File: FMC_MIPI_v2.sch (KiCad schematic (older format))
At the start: 0 parts

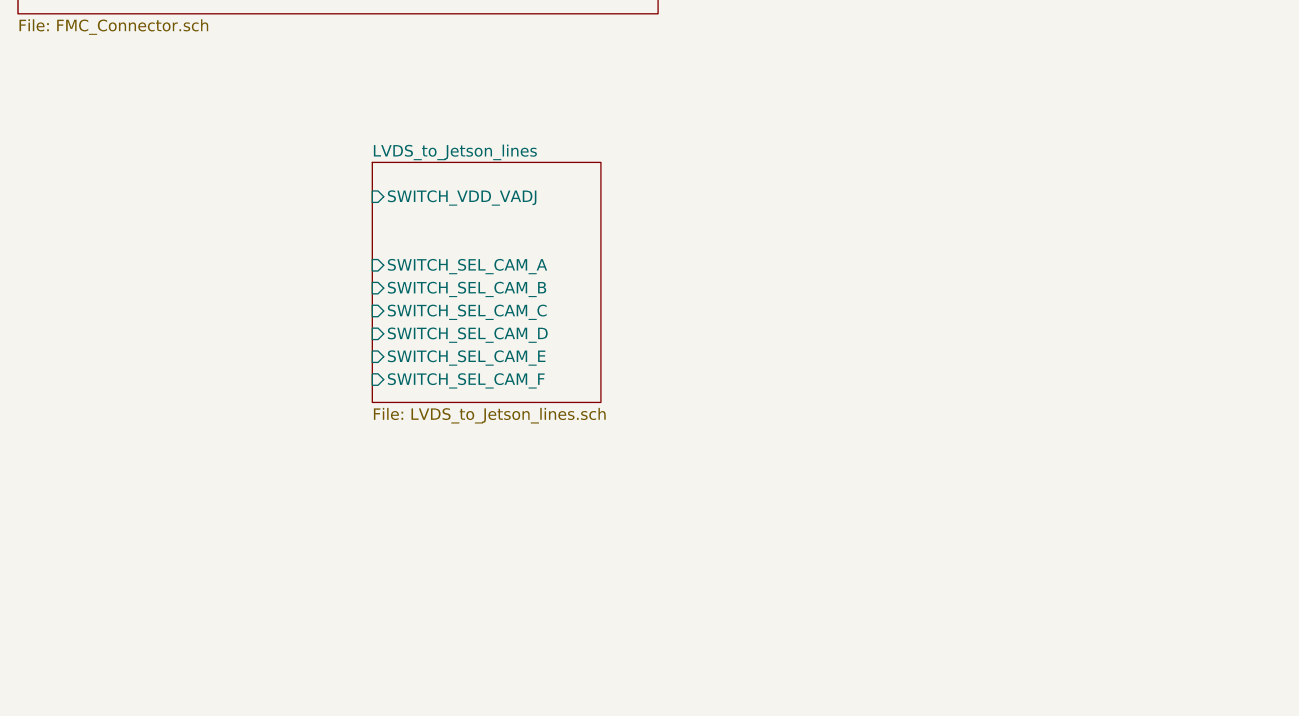
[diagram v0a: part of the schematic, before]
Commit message: Good, before replacing the swithches to TI ones
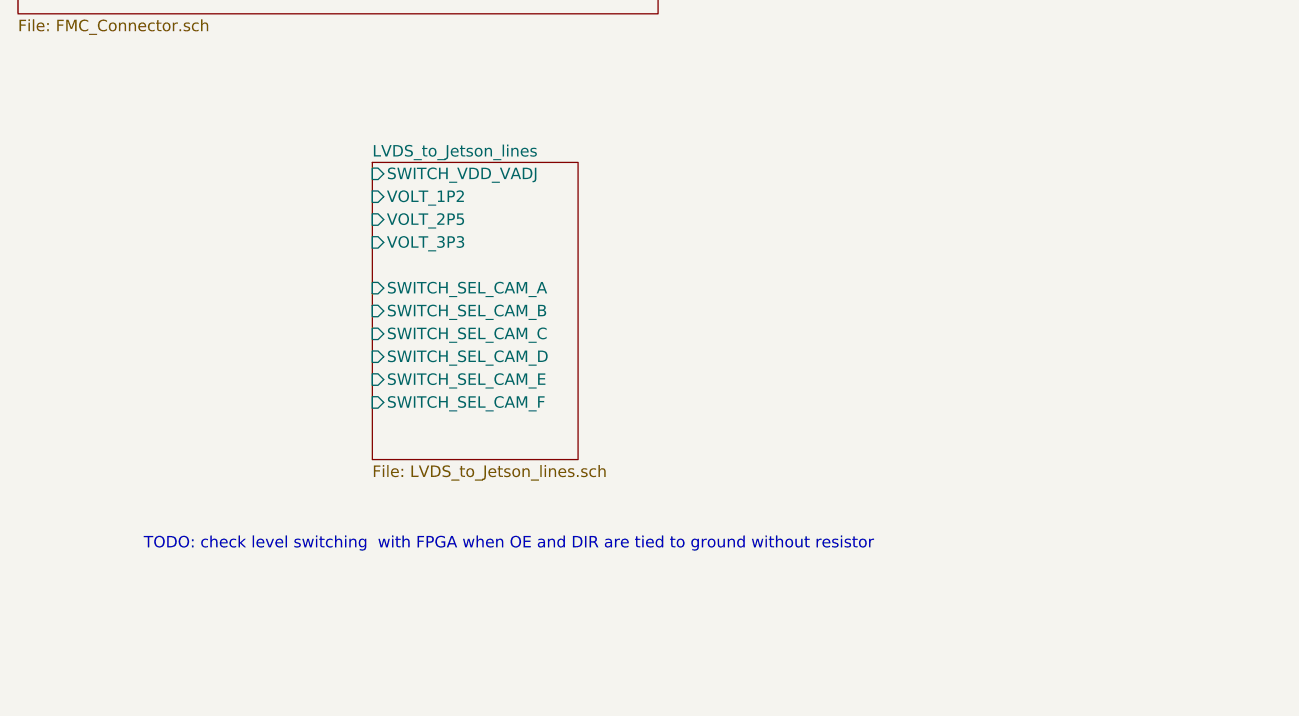
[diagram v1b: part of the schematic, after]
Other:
- note added: "TODO: check level switching with FPGA when OE and DIR are tied to ground without resistor"
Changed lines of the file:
@@
 $Descr A4 11693 8268
 encoding utf-8
-Sheet 1 46
+Sheet 1 32
 Title ""
 Date ""
@@
 $EndSheet
 $Comp
-L FMC_MIPI_v2:Earth #PWR0101
+L FMC_MIPI_v2:Earth #PWR01
 U 1 1 61B01356
 P 5950 5600
-F 0 "#PWR0101" H 5950 5350 50  0001 C CNN
+F 0 "#PWR01" H 5950 5350 50  0001 C CNN
 F 1 "Earth" H 5950 5450 50  0001 C CNN
 F 2 "" H 5950 5600 50  0001 C CNN
@@
 PI3WVR646 is 10 lines!!! use it!! when available\n\nPI3WVR626	PI3WVR626 Datasheet	2:1 MIPI 2-Data Lane, 1.5Gbps(D-PHY) Switch\nPI3WVR628	PI3WVR628 Datasheet	2:1 MIPI 2-Data Lane, 4.5Gbps(D-PHY) switch\nPI3WVR646	PI3WVR646 Datasheet	2:1 MIPI 4-Data Lane, 2.5Gbps(D-PHY) Switch\nPI3WVR648	PI3WVR648 Product brief	2:1 MIPI 4-Data Lane, 4.5Gbps(D-PHY) Switch\n		\n\n\n\nConsider using SNx5DPHY440SS retimer (no stock)
 $Sheet
-S 2450 2950 1000 1050
+S 2450 2950 900  1300
 U 6191D89C
 F0 "LVDS_to_Jetson_lines" 50
 F1 "LVDS_to_Jetson_lines.sch" 50
-F2 "SWITCH_VDD_VADJ" I L 2450 3100 50
-F3 "SWITCH_SEL_CAM_A" I L 2450 3400 50
-F4 "SWITCH_SEL_CAM_B" I L 2450 3500 50
-F5 "SWITCH_SEL_CAM_C" I L 2450 3600 50
-F6 "SWITCH_SEL_CAM_D" I L 2450 3700 50
-F7 "SWITCH_SEL_CAM_E" I L 2450 3800 50
-F8 "SWITCH_SEL_CAM_F" I L 2450 3900 50
+F2 "SWITCH_VDD_VADJ" I L 2450 3000 50
+F3 "SWITCH_SEL_CAM_A" I L 2450 3500 50
+F4 "SWITCH_SEL_CAM_B" I L 2450 3600 50
+F5 "SWITCH_SEL_CAM_C" I L 2450 3700 50
+F6 "SWITCH_SEL_CAM_D" I L 2450 3800 50
+F7 "SWITCH_SEL_CAM_E" I L 2450 3900 50
+F8 "SWITCH_SEL_CAM_F" I L 2450 4000 50
+F9 "VOLT_1P2" I L 2450 3100 50
+F10 "VOLT_2P5" I L 2450 3200 50
+F11 "VOLT_3P3" I L 2450 3300 50
 $EndSheet
+Text Notes 1450 4650 0    50   ~ 0
+TODO: check level switching  with FPGA when OE and DIR are tied to ground without resistor
 $EndSCHEMATC

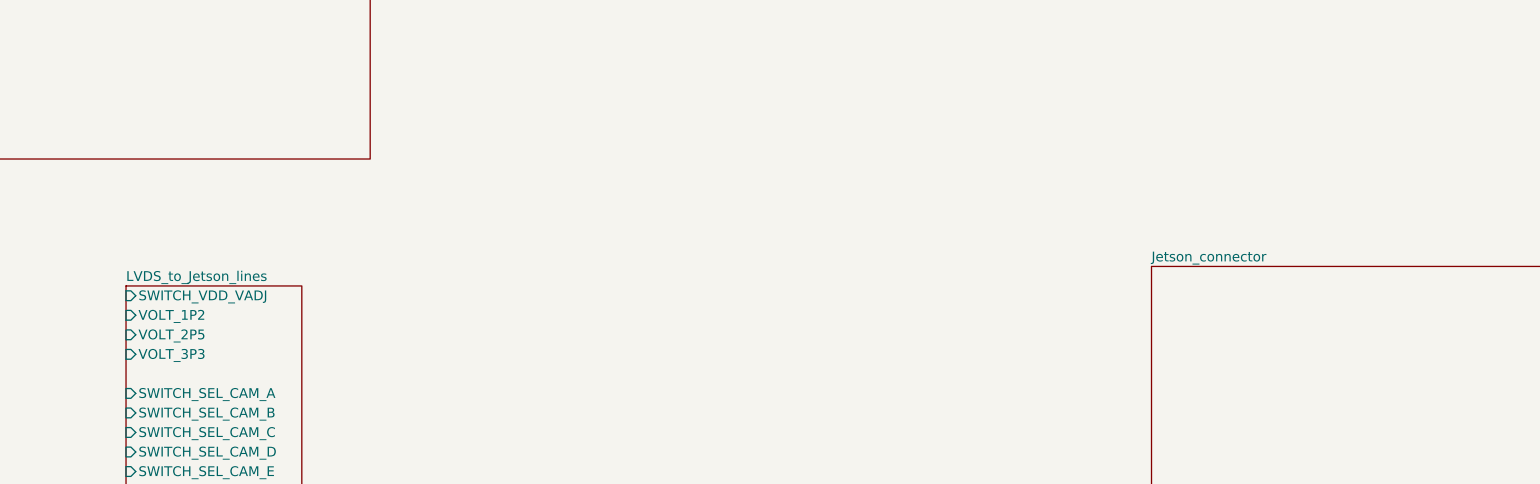
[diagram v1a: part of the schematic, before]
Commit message: good, added re-driver
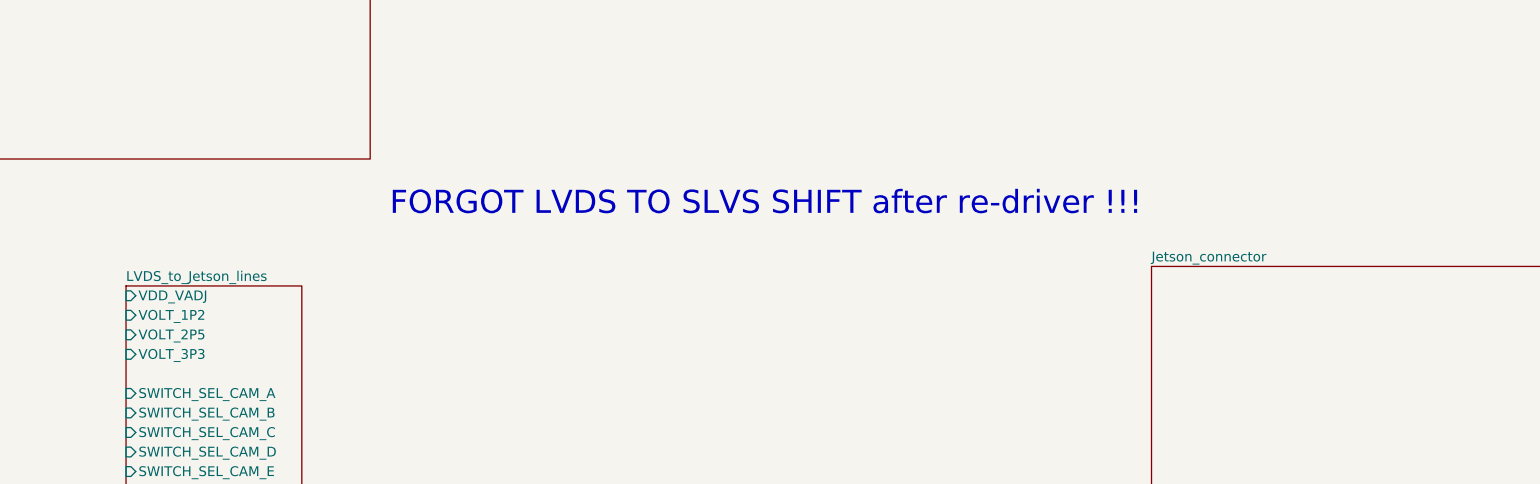
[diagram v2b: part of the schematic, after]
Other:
- note added: "FORGOT LVDS TO SLVS SHIFT after re-driver !!!"
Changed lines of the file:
@@
 $Descr A4 11693 8268
 encoding utf-8
-Sheet 1 32
+Sheet 1 7
 Title ""
 Date ""
@@
 F0 "LVDS_to_Jetson_lines" 50
 F1 "LVDS_to_Jetson_lines.sch" 50
-F2 "SWITCH_VDD_VADJ" I L 2450 3000 50
+F2 "VDD_VADJ" I L 2450 3000 50
 F3 "SWITCH_SEL_CAM_A" I L 2450 3500 50
 F4 "SWITCH_SEL_CAM_B" I L 2450 3600 50
@@
 Text Notes 1450 4650 0    50   ~ 0
 TODO: check level switching  with FPGA when OE and DIR are tied to ground without resistor
+Text Notes 3800 2600 0    118  ~ 0
+FORGOT LVDS TO SLVS SHIFT after re-driver !!!
 $EndSCHEMATC

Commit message: good, before reducing
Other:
- note added: "For I2C level shifting we will use TCA9406"
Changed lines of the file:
@@
 $Descr A4 11693 8268
 encoding utf-8
-Sheet 1 7
+Sheet 1 15
 Title ""
 Date ""
@@
 F1 "LVDS_to_Jetson_lines.sch" 50
 F2 "VDD_VADJ" I L 2450 3000 50
-F3 "SWITCH_SEL_CAM_A" I L 2450 3500 50
+F3 "SWITCH_CAM_C_D" I L 2450 3500 50
 F4 "SWITCH_SEL_CAM_B" I L 2450 3600 50
 F5 "SWITCH_SEL_CAM_C" I L 2450 3700 50
@@
 Text Notes 3800 2600 0    118  ~ 0
 FORGOT LVDS TO SLVS SHIFT after re-driver !!!
+Text Notes 1450 5250 0    50   ~ 0
+For I2C level shifting we will use TCA9406
 $EndSCHEMATC

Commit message: before re-arranging
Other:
- note added: "Add another solution using PI3WVR646 or similar switch"
- note added: "For low power (LP) lines use only one livel shifter, and connect the output to multiple\nswitches. If needed, merge to pins to get more power."
- note added: "Looks like we need 15 Ohm resistor after re-driver!!! With 12 Ohm the swing is only 115 mVolt!!!\n\nCheck it!!!\n\nFor direct convertion BLVDS to SLVS we will use 9.1 Ohm resistor .Oct 10, 2022"
- note added: "To switch cameras simply use: TS5MP645\n\nhttps://www.ti.com/lit/ds/symlink/ts5mp645.pdf?ts=1639239156409&ref_url=https%253A%252F%252Fwww.ti.com%252Fproduct%252FTS5MP645"
- note removed: "FORGOT LVDS TO SLVS SHIFT after re-driver !!!"
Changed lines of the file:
@@
 F1 "LVDS_to_Jetson_lines.sch" 50
 F2 "VDD_VADJ" I L 2450 3000 50
-F3 "SWITCH_CAM_C_D" I L 2450 3500 50
-F4 "SWITCH_SEL_CAM_B" I L 2450 3600 50
-F5 "SWITCH_SEL_CAM_C" I L 2450 3700 50
-F6 "SWITCH_SEL_CAM_D" I L 2450 3800 50
-F7 "SWITCH_SEL_CAM_E" I L 2450 3900 50
-F8 "SWITCH_SEL_CAM_F" I L 2450 4000 50
-F9 "VOLT_1P2" I L 2450 3100 50
-F10 "VOLT_2P5" I L 2450 3200 50
-F11 "VOLT_3P3" I L 2450 3300 50
+F3 "SWITCH_HS_LV_CAM_C" I L 2450 3500 50
+F4 "VOLT_1P2" I L 2450 3100 50
+F5 "VOLT_2P5" I L 2450 3200 50
+F6 "VOLT_3P3" I L 2450 3300 50
 $EndSheet
 Text Notes 1450 4650 0    50   ~ 0
 TODO: check level switching  with FPGA when OE and DIR are tied to ground without resistor
-Text Notes 3800 2600 0    118  ~ 0
-FORGOT LVDS TO SLVS SHIFT after re-driver !!!
 Text Notes 1450 5250 0    50   ~ 0
 For I2C level shifting we will use TCA9406
+Text Notes -100 -400 0    118  ~ 0
+To switch cameras simply use: TS5MP645\n\nhttps://www.ti.com/lit/ds/symlink/ts5mp645.pdf?ts=1639239156409&ref_url=https%253A%252F%252Fwww.ti.com%252Fproduct%252FTS5MP645
+Text Notes 1450 5750 0    50   ~ 0
+Add another solution using PI3WVR646 or similar switch
+Text Notes 1450 6050 0    50   ~ 0
+For low power (LP) lines use only one livel shifter, and connect the output to multiple\nswitches. If needed, merge to pins to get more power.
+Text Notes 4100 1850 0    118  ~ 24
+Looks like we need 15 Ohm resistor after re-driver!!! With 12 Ohm the swing is only 115 mVolt!!!\n\nCheck it!!!\n\nFor direct convertion BLVDS to SLVS we will use 9.1 Ohm resistor .Oct 10, 2022
 $EndSCHEMATC

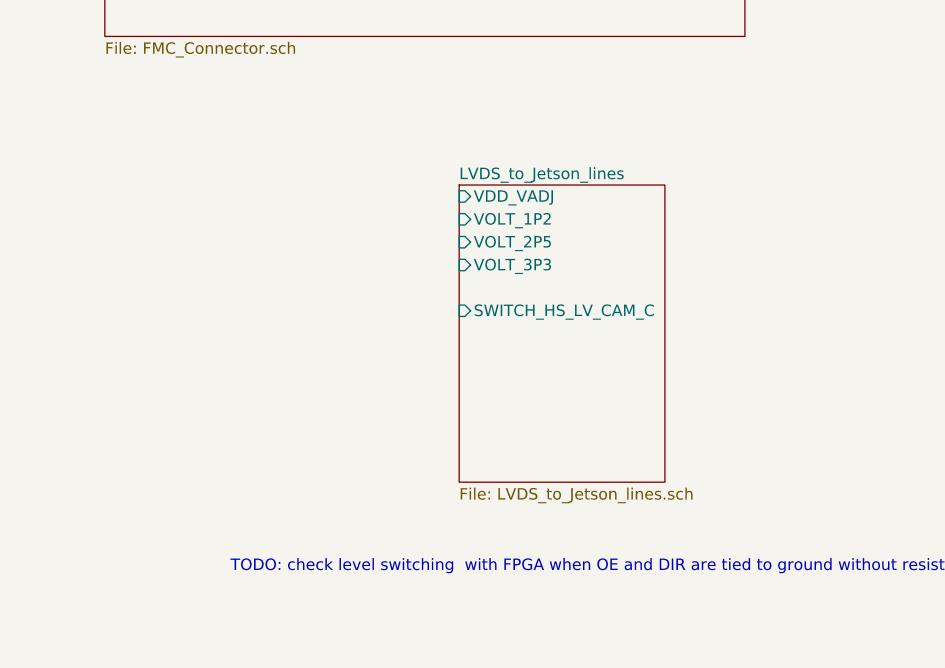
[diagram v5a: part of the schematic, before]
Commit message: fixed 3.3 volt level shifter
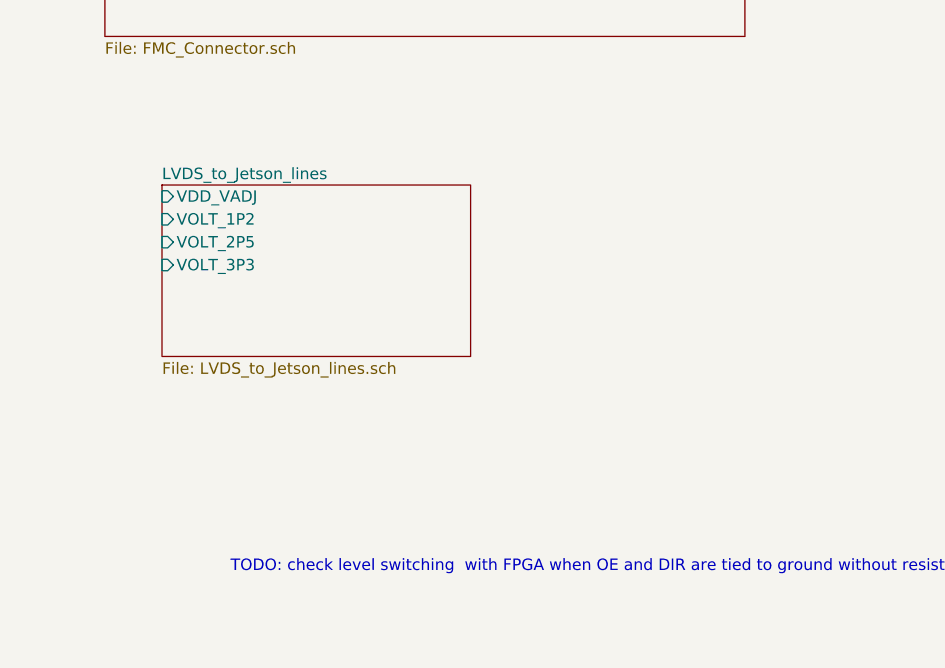
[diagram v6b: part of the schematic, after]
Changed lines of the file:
@@
 $Descr A4 11693 8268
 encoding utf-8
-Sheet 1 16
+Sheet 1 10
 Title ""
 Date ""
@@
 PI3WVR646 is 10 lines!!! use it!! when available\n\nPI3WVR626	PI3WVR626 Datasheet	2:1 MIPI 2-Data Lane, 1.5Gbps(D-PHY) Switch\nPI3WVR628	PI3WVR628 Datasheet	2:1 MIPI 2-Data Lane, 4.5Gbps(D-PHY) switch\nPI3WVR646	PI3WVR646 Datasheet	2:1 MIPI 4-Data Lane, 2.5Gbps(D-PHY) Switch\nPI3WVR648	PI3WVR648 Product brief	2:1 MIPI 4-Data Lane, 4.5Gbps(D-PHY) Switch\n		\n\n\n\nConsider using SNx5DPHY440SS retimer (no stock)
 $Sheet
-S 2450 2950 900  1300
+S 1150 2950 1350 750
 U 6191D89C
 F0 "LVDS_to_Jetson_lines" 50
 F1 "LVDS_to_Jetson_lines.sch" 50
-F2 "VDD_VADJ" I L 2450 3000 50
-F3 "SWITCH_HS_LV_CAM_C" I L 2450 3500 50
-F4 "VOLT_1P2" I L 2450 3100 50
-F5 "VOLT_2P5" I L 2450 3200 50
-F6 "VOLT_3P3" I L 2450 3300 50
+F2 "VDD_VADJ" I L 1150 3000 50
+F3 "VOLT_1P2" I L 1150 3100 50
+F4 "VOLT_2P5" I L 1150 3200 50
+F5 "VOLT_3P3" I L 1150 3300 50
 $EndSheet
 Text Notes 1450 4650 0    50   ~ 0

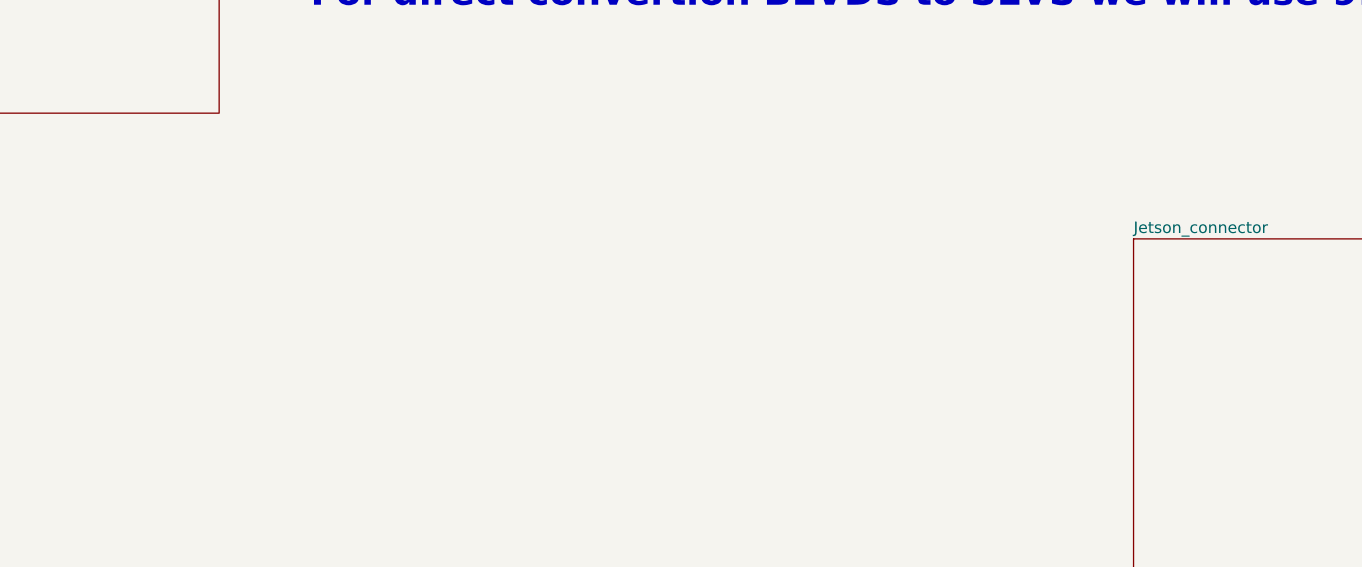
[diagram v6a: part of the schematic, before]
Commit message: added EEPROM
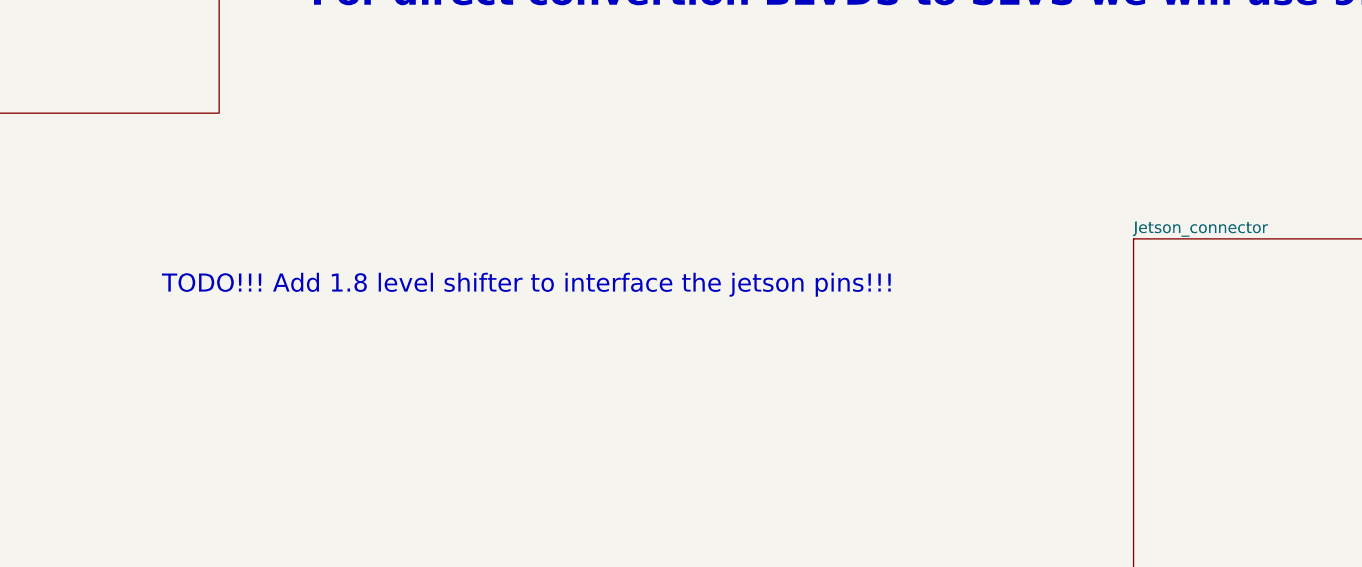
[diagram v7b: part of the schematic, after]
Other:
- note added: "TODO!!! Add 1.8 level shifter to interface the jetson pins!!!"
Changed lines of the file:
@@
 Text Notes 4100 1850 0    118  ~ 24
 Looks like we need 15 Ohm resistor after re-driver!!! With 12 Ohm the swing is only 115 mVolt!!!\n\nCheck it!!!\n\nFor direct convertion BLVDS to SLVS we will use 9.1 Ohm resistor .Oct 10, 2022
+Text Notes 3450 3100 0    79   ~ 0
+TODO!!! Add 1.8 level shifter to interface the jetson pins!!!
 $EndSCHEMATC
